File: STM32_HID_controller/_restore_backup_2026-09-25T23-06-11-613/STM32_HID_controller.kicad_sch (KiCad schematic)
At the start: 57 parts, among them J1 USB_B_Micro, J2 Conn_01x04_Pin, J3 Conn_01x03_Pin, J5 Conn_01x03_Pin, SW1 SW_SPDT, SW10 SW_Push, SW11 SW_Push, SW14 SW_Push, SW2 SW_Push, SW3 SW_Push, SW6 SW_Push, SW7 SW_Push, SW8 SW_Push, SW9 SW_Push, U1 STM32F446RETx, U2 AMS1117-3.3, U4 joystick_right, U5 joystick_left, U7 MPU-6050, Y1 8MHz

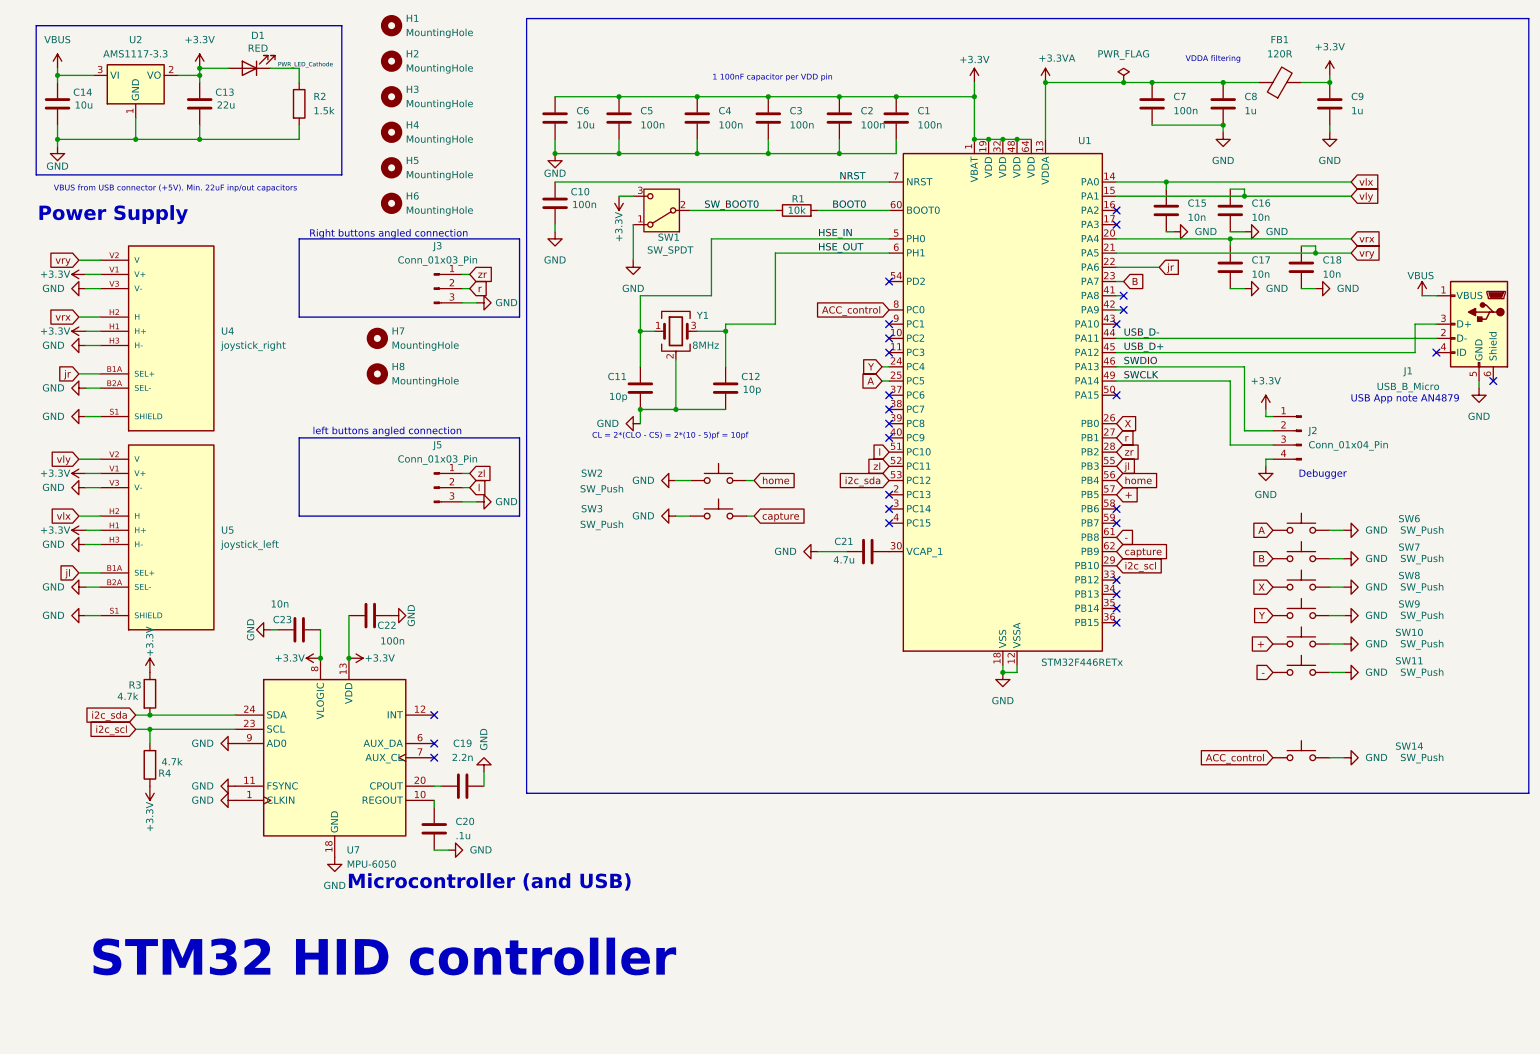
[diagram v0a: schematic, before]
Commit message: updated for switch config
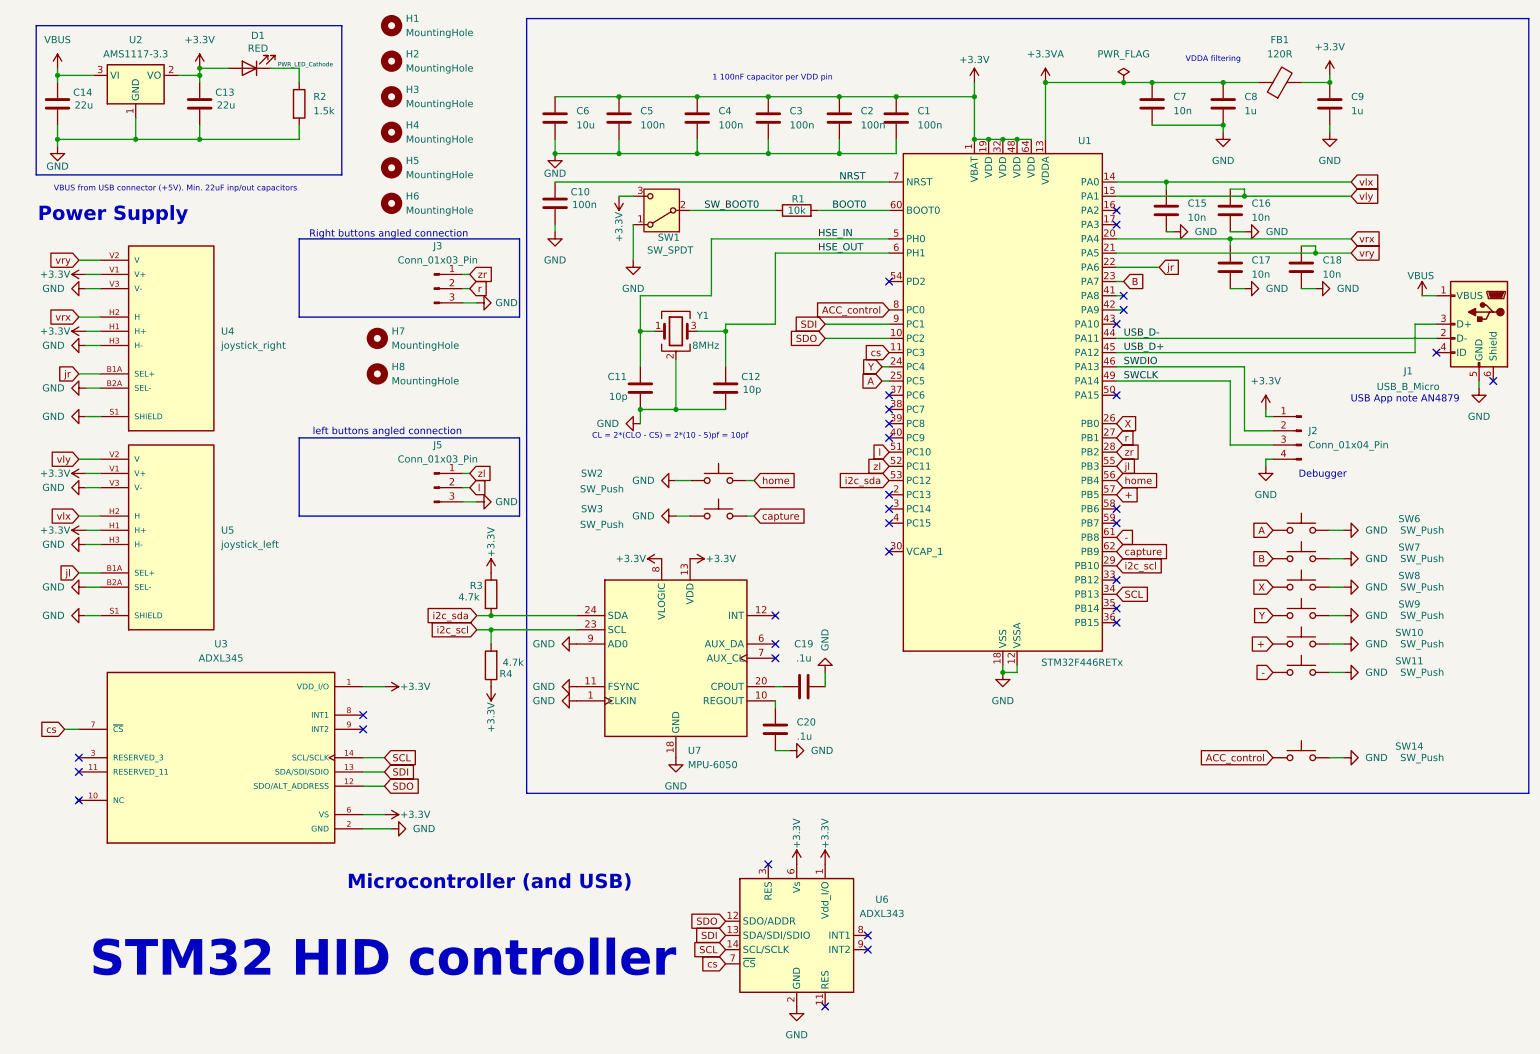
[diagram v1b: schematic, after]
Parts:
- removed C21: 4.7u, Capacitor_SMD:C_0402_1005Metric, symbol Device:C
- removed C22: 100n, Capacitor_SMD:C_0402_1005Metric, symbol Device:C
- removed C23: 10n, Capacitor_SMD:C_0402_1005Metric, symbol Device:C
- added U3: ADXL345, ADXL345:PQFN80P500X300X100-14N, symbol ADXL345:ADXL345
- added U6: ADXL343, Package_LGA:LGA-14_3x5mm_P0.8mm_LayoutBorder1x6y, symbol Sensor_Motion:ADXL343
- C14: value 10u -> 22u
- C19: value 2.2n -> .1u
- C7: value 100n -> 10n
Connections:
- net +3.3V: now also U3.1 (VDD_I/O), U3.6 (VS), U6.1 (Vdd_I/O), U6.6 (Vs)
- net GND: now also U3.2 (GND), U3.4 (GND), U3.5 (GND), U6.2 (GND), U6.4 (GND), U6.5 (GND)
- net SDO: now reaches U1.10 (PC2)
- net SDO: now also U3.12 (SDO/ALT_ADDRESS), U6.12 (SDO/ADDR)
- net cs: now reaches U1.11 (PC3)
- net cs: now also U3.7 (~{CS}), U6.7 (~{CS})
- net SCL: now reaches U1.34 (PB13)
- net SCL: now also U3.14 (SCL/SCLK), U6.14 (SCL/SCLK)
- net SDI: now reaches U1.9 (PC1)
- net SDI: now also U3.13 (SDA/SDI/SDIO), U6.13 (SDA/SDI/SDIO)
- no-connect marks 28 -> 34
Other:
- moved on the sheet: C19, C20, R3, R4, U7
